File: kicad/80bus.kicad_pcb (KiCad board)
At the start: 2 copper layers, 140 x 100 mm, 67 parts, among them IC1 NE555P, IC2 4049, IC3 4040, T1 22uf, T2 22uf, T3 2.2uf, T4 2.2uf

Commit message: Remove unused files, tweak design layout
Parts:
- moved T1 5.03 mm to (240.9, 50.6), turned to 180 degrees
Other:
- board text added: "Errata 1.1 -> 1.2 R10 should be 820K not 820 Add missing component values Tidy silk screening T1 Swapped orientation"
- board text removed: "Errata 1.1 -> 1.2 R10 should be 820K not 820 Add missing component values Tidy silk screening"
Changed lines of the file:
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@@
   (title_block
     (title "Nascom 2708 / 2716 EPROM programmer")
-    (date "2023-05-01")
-    (rev "1.1")
+    (date "2023-06-18")
+    (rev "1.2")
   )
   (layers
@@
         (effects (font (size 1 1) (thickness 0.15)))
     )
-    (fp_text value "TestPoint" (at 3.2258 0) (layer "F.SilkS")
+    (fp_text value "TestPoint" (at 5.197849 -0.069626) (layer "F.SilkS")
         (effects (font (size 1 1) (thickness 0.15)))
     )
@@
   )
   (footprint "Capacitor_THT:C_Disc_D5.0mm_W2.5mm_P5.00mm" (layer "F.Cu")
-    (at 235.879 50.9016)
+    (at 240.899099 50.604982 180)
     (descr "C, Disc series, Radial, pin pitch=5.00mm, , diameter*width=5*2.5mm^2, Capacitor, http://cdn-reichelt.de/documents/datenblatt/B300/DS_KERKO_TC.pdf")
     (tags "C Disc series Radial pin pitch 5.00mm  diameter 5mm width 2.5mm Capacitor")
@@
     (property "ki_keywords" "cap capacitor")
     (attr through_hole)
-    (fp_text reference "T1" (at -1.8942 0.889) (layer "F.SilkS")
+    (fp_text reference "T1" (at 7.046759 0.004686) (layer "F.SilkS")
         (effects (font (size 1 1) (thickness 0.15)))
     )
-    (fp_text value "22uf" (at 8.0372 -0.0254) (layer "F.SilkS")
+    (fp_text value "22uf" (at -3.020793 0.047447) (layer "F.SilkS")
         (effects (font (size 1 1) (thickness 0.15)))
     )
@@
     (fp_line (start 5 1.25) (end 5 -1.25)
       (stroke (width 0.1) (type solid)) (layer "F.Fab"))
-    (pad "1" thru_hole circle (at 0 0) (size 1.6 1.6) (drill 0.8) (layers "*.Cu" "*.Mask")
+    (pad "1" thru_hole circle (at 0 0 180) (size 1.6 1.6) (drill 0.8) (layers "*.Cu" "*.Mask")
       (net 4 "Net-(D1-K)") (pintype "passive"))
-    (pad "2" thru_hole circle (at 5 0) (size 1.6 1.6) (drill 0.8) (layers "*.Cu" "*.Mask")
+    (pad "2" thru_hole circle (at 5 0 180) (size 1.6 1.6) (drill 0.8) (layers "*.Cu" "*.Mask")
       (net 9 "SWITCHED 12V") (pintype "passive"))
     (model "${KICAD6_3DMODEL_DIR}/Capacitor_THT.3dshapes/C_Disc_D5.0mm_W2.5mm_P5.00mm.wrl"
@@
   (gr_line (start 292 148) (end 152 148)
     (stroke (width 0.05) (type solid)) (layer "Edge.Cuts"))
-  (gr_text "Errata 1.1 -> 1.2\n	R10 should be 820K not 820\n	Add missing component values\n	Tidy silk screening" (at 206.496717 107.774653) (layer "B.SilkS")
+  (gr_text "Errata 1.1 -> 1.2\n	R10 should be 820K not 820\n	Add missing component values\n	Tidy silk screening\n	T1 Swapped orientation" (at 204.082977 115.271121) (layer "B.SilkS")
     (effects (font (size 1.5 1.5) (thickness 0.3) bold) (justify left bottom mirror))
   )
@@
     (effects (font (size 1.5 1.5) (thickness 0.3) bold) (justify left bottom))
   )
-  (gr_text "+" (at 242.274664 48.912499) (layer "F.SilkS")
+  (gr_text "+" (at 242.986767 48.991784) (layer "F.SilkS")
     (effects (font (size 1.5 1.5) (thickness 0.3)))
   )
@@
     (effects (font (size 1 1) (thickness 0.15)) (justify left bottom))
   )
-  (gr_text "SOURCE EPROM" (at 211.4296 132.8928 90) (layer "F.SilkS")
+  (gr_text "SOURCE EPROM" (at 212.036135 135.828837 90) (layer "F.SilkS")
     (effects (font (size 1.5 1.5) (thickness 0.3) bold) (justify left bottom))
   )
@@
     (effects (font (size 1 1) (thickness 0.15)) (justify left bottom))
   )
-  (gr_text "TARGET EPROM" (at 236.9566 132.461 90) (layer "F.SilkS")
+  (gr_text "TARGET EPROM" (at 259.27556 138.310909 90) (layer "F.SilkS")
     (effects (font (size 1.5 1.5) (thickness 0.3) bold) (justify left bottom))
   )
@@
   (segment (start 257.6576 66.929) (end 248.6914 66.929) (width 0.5) (layer "F.Cu") (net 4))
   (segment (start 257.6576 66.929) (end 257.6576 68.1482) (width 1) (layer "B.Cu") (net 4))
-  (segment (start 242.062 52.0846) (end 242.062 60.2996) (width 0.5) (layer "B.Cu") (net 4))
-  (segment (start 240.879 50.9016) (end 242.062 52.0846) (width 0.5) (layer "B.Cu") (net 4))
-  (segment (start 242.062 60.2996) (end 248.666 66.9036) (width 0.5) (layer "B.Cu") (net 4))
+  (segment (start 242.062 60.2996) (end 242.062 51.767883) (width 0.5) (layer "B.Cu") (net 4))
+  (segment (start 242.062 51.767883) (end 240.899099 50.604982) (width 0.5) (layer "B.Cu") (net 4))
   (segment (start 257.6576 68.1482) (end 260.1722 70.6628) (width 1) (layer "B.Cu") (net 4))
+  (segment (start 248.666 66.9036) (end 242.062 60.2996) (width 0.5) (layer "B.Cu") (net 4))
   (segment (start 267.1426 143.1798) (end 264.7296 145.5928) (width 1) (layer "F.Cu") (net 5))
   (segment (start 183.0832 132.2832) (end 178.8568 132.2832) (width 1) (layer "F.Cu") (net 5))

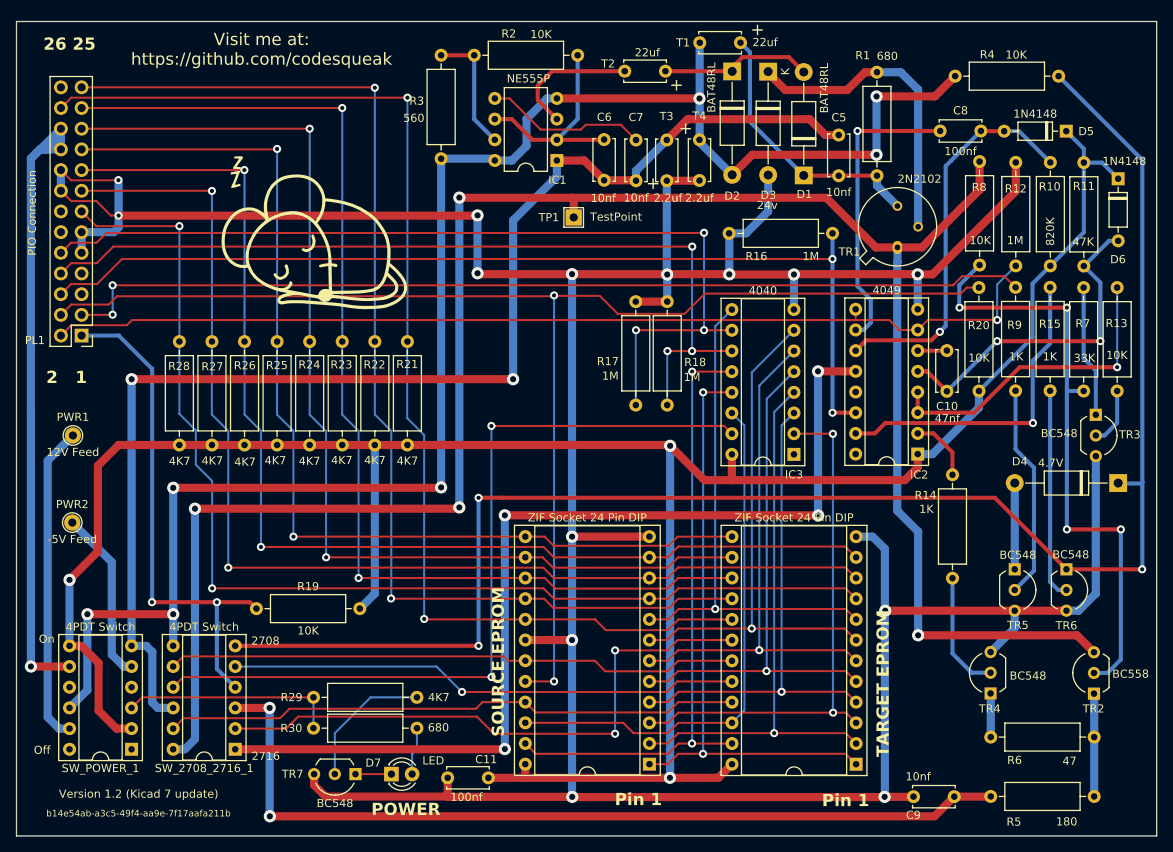
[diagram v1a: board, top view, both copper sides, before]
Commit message: Kicad 9 and Docs
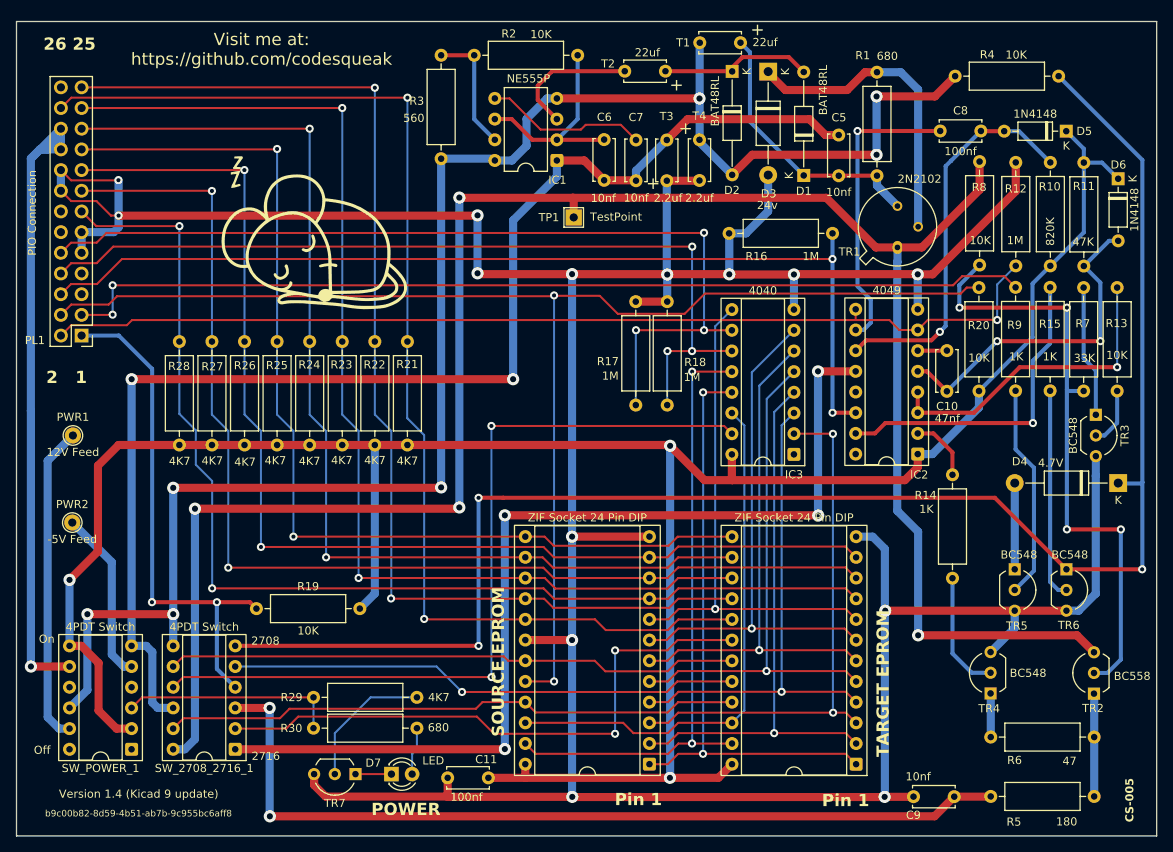
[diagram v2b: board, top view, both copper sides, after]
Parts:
- added G001: LOGO, 80bus:qr code, B.Cu at (170.4, 57.6)
- D1, D2: footprint Diode_THT:D_DO-41_SOD81_P12.70mm_Horizontal -> Diode_THT:D_DO-35_SOD27_P12.70mm_Horizontal
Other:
- board text added: "CS-005"
- board text added: "Documentation -->"
- board text added: "Version 1.4 (Kicad 9 update)"
- board text added: "b9c00b82-8d59-4b51-ab7b-9c955bc6aff8"
- board text removed: "Version 1.2 (Kicad 7 update)"
- board text removed: "b14e54ab-a3c5-49f4-aa9e-7f17aafa211b"
